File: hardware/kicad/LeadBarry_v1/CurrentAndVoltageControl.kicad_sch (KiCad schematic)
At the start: 27 parts, among them J1 Screw_Terminal_01x02, Q1 SS9014, U2 INA3221_Module, U3 LM2596S_Module

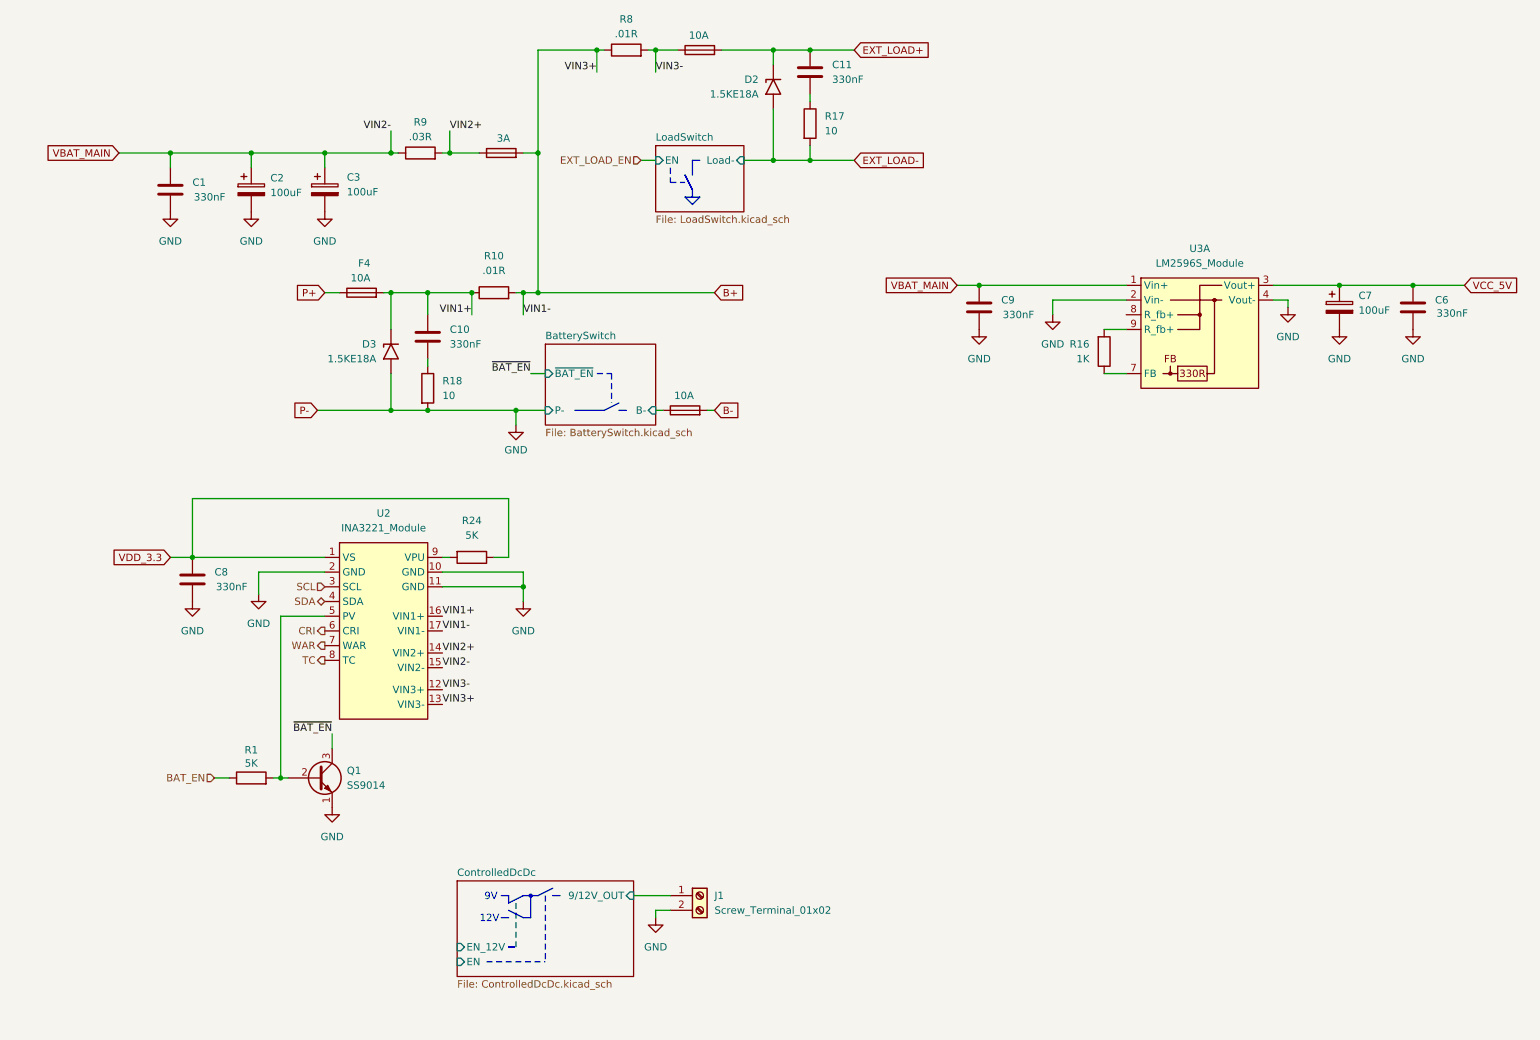
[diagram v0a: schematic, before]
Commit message: fix: pwm-controlled dc-dc output voltage
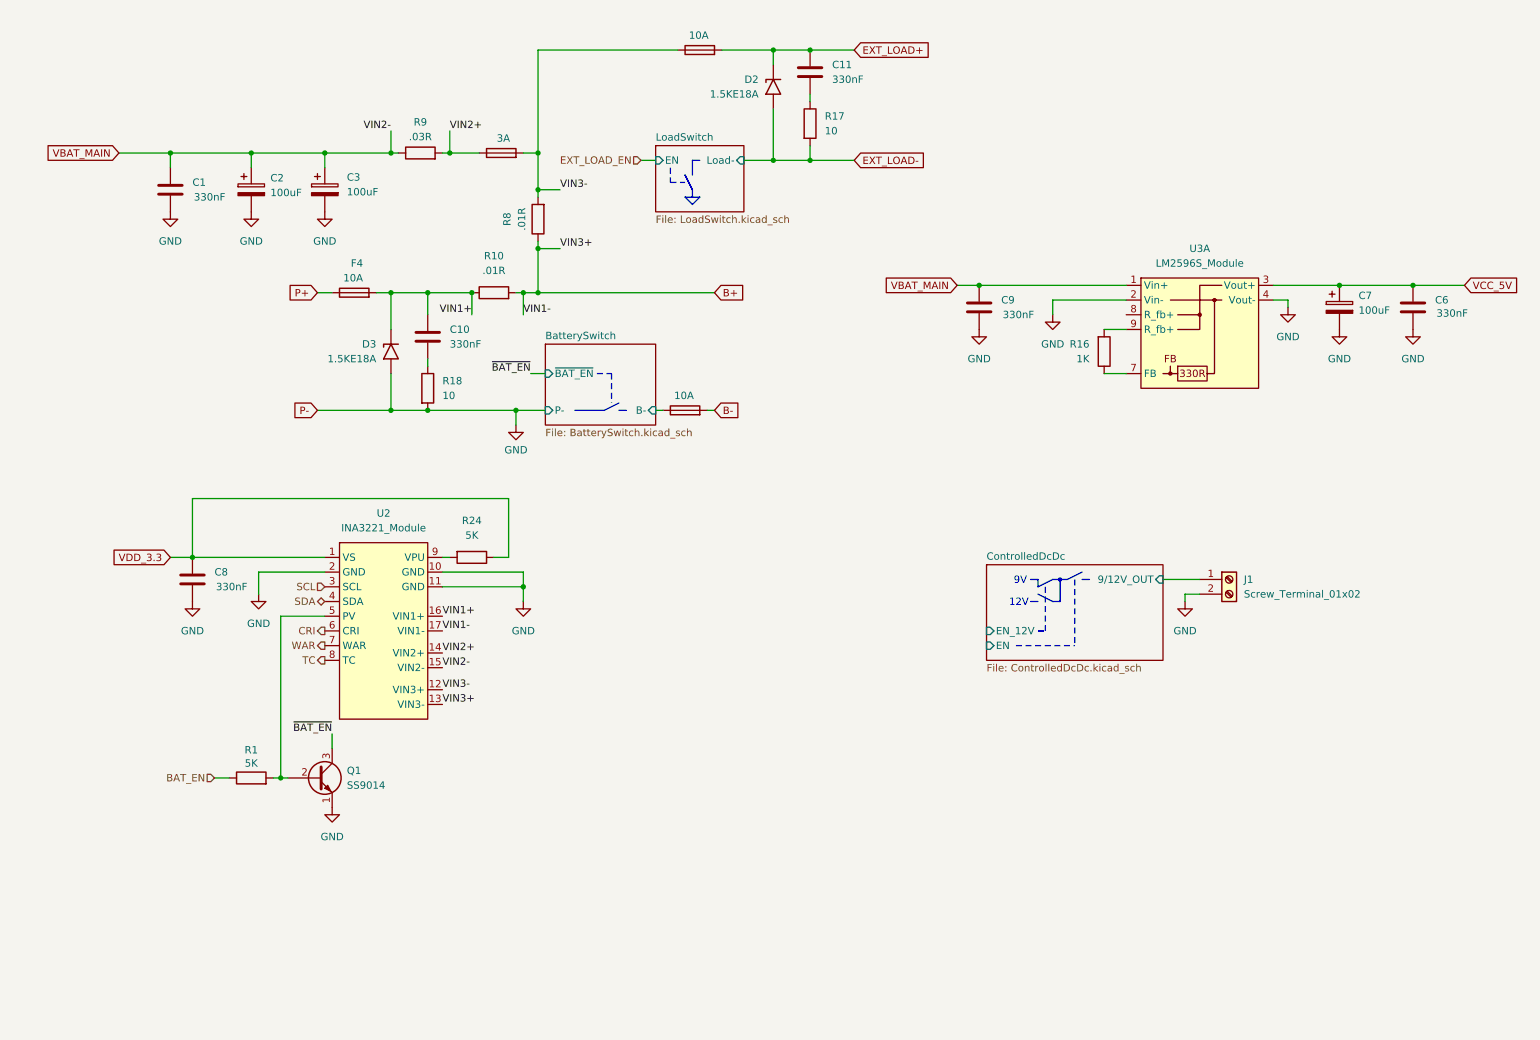
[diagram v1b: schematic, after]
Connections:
- net B+: no longer F1.2
- net VIN3-: now also F1.2
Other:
- moved on the sheet: F4, J1

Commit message: Revert "fix: pwm-controlled dc-dc output voltage"
This reverts commit b0b1c2266e3c7e9cf1a5c295a0eb9d631b1ef3e0.
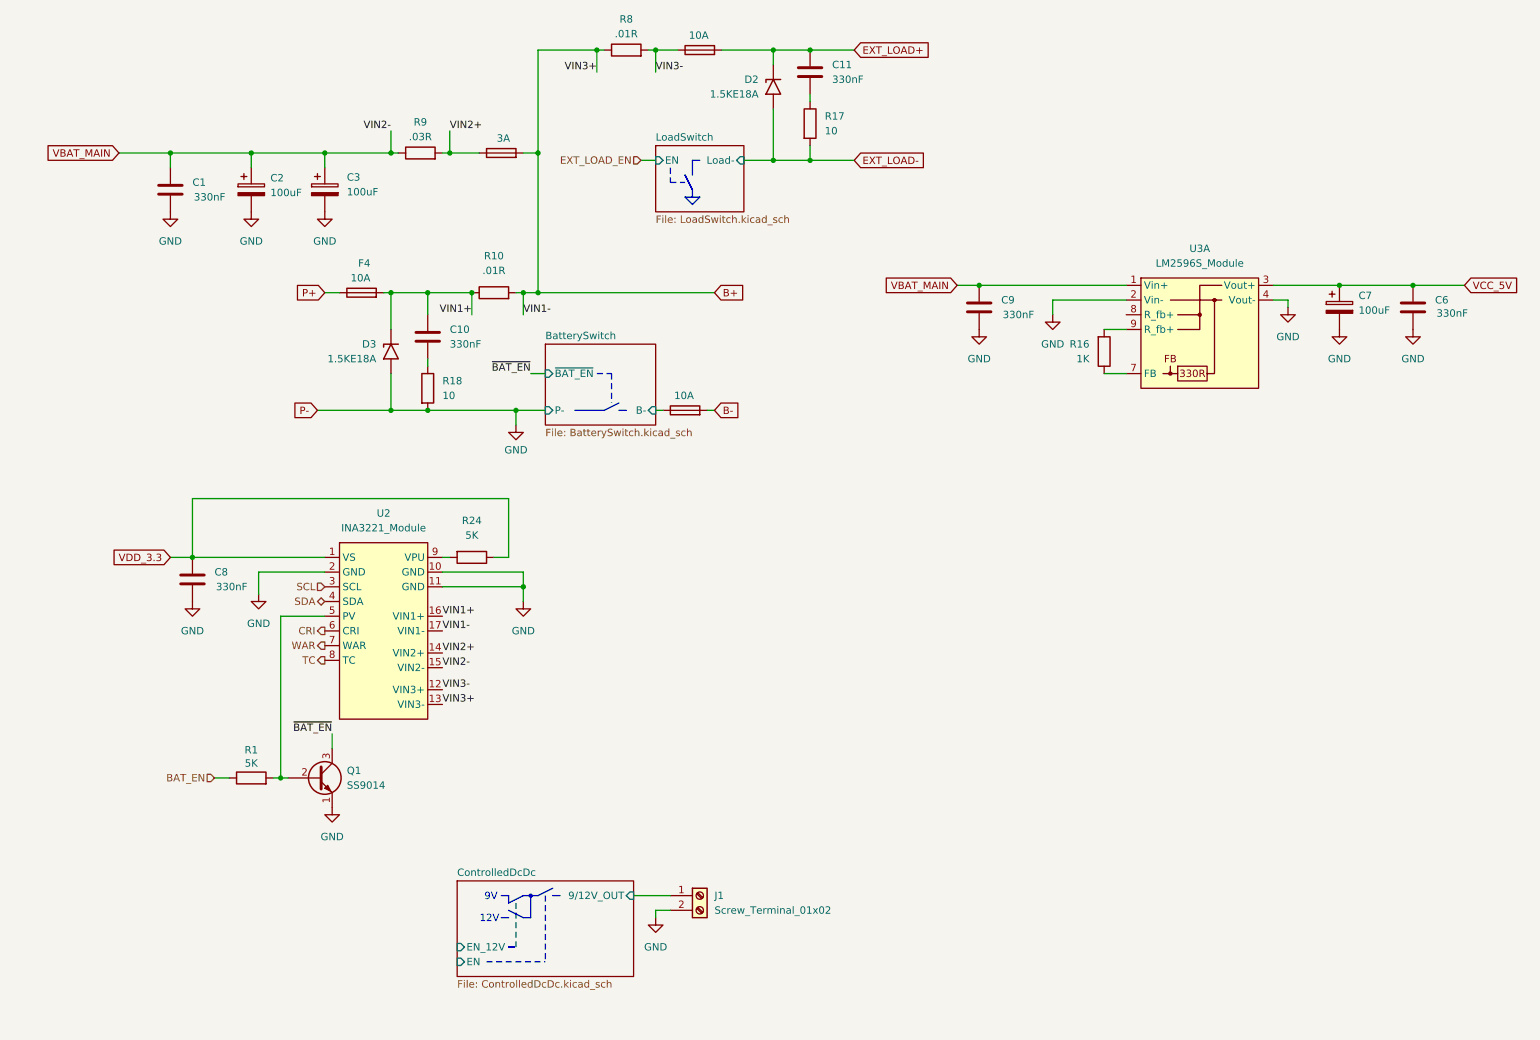
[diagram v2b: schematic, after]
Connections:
- net B+: now also F1.2
- net VIN3-: no longer F1.2
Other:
- moved on the sheet: F4, J1

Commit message: doc: refactored and enhanced
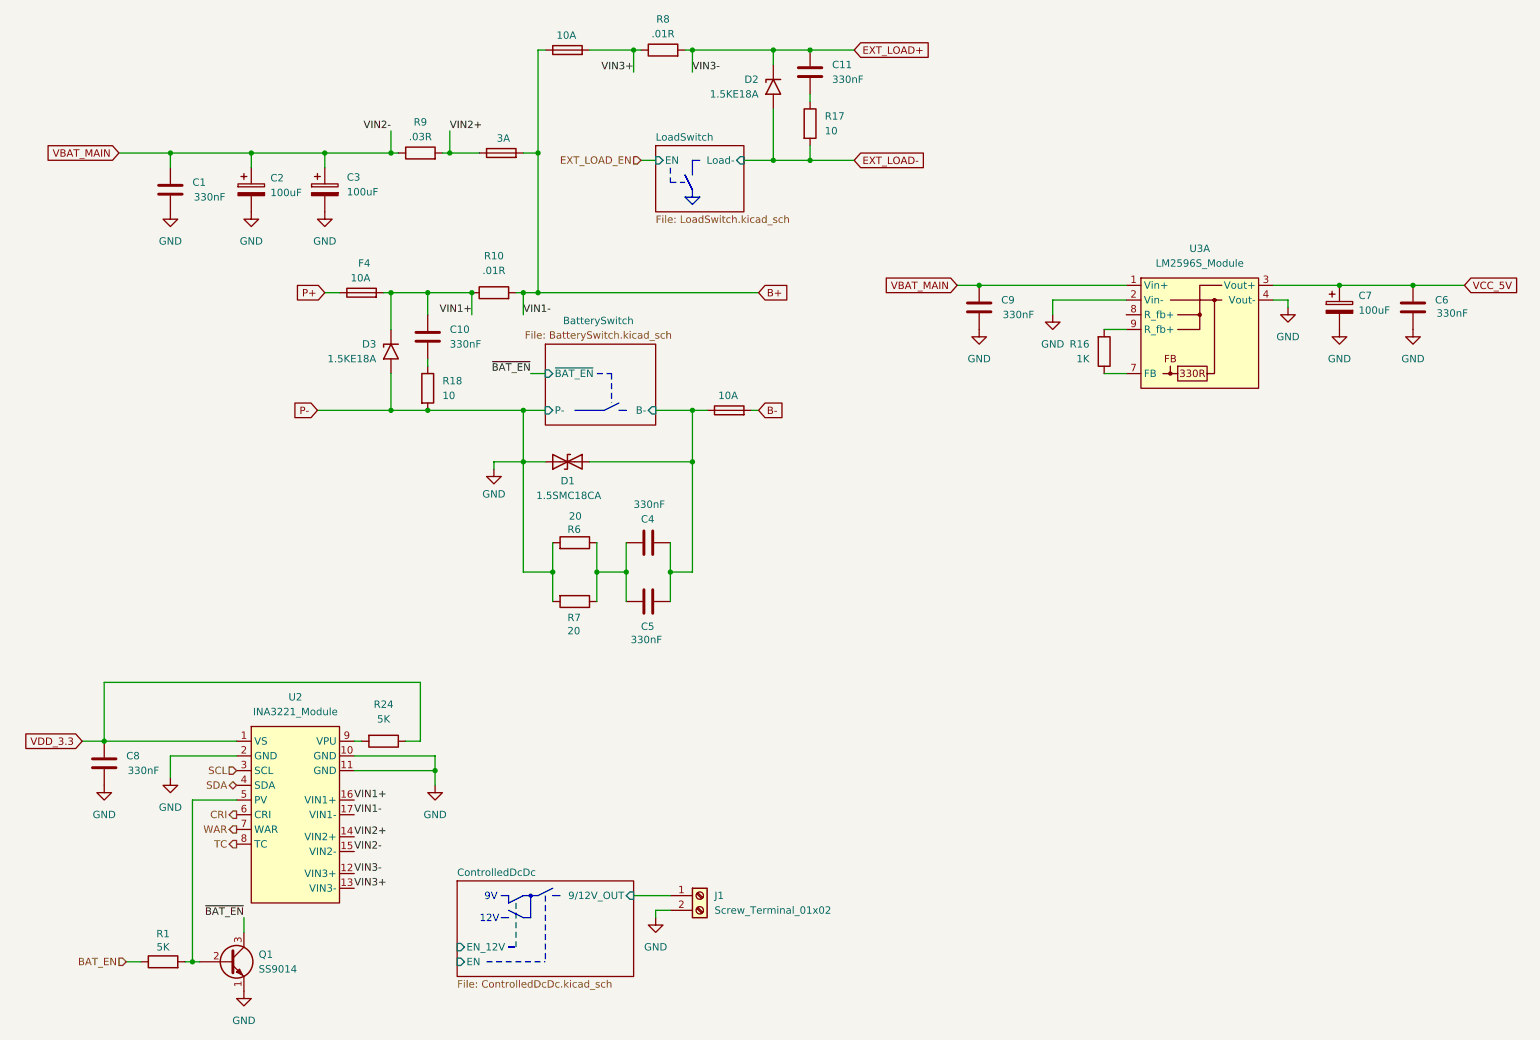
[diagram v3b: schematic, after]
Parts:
- added C4, C5: 330nF, symbol Device:C
- added D1: 1.5SMC18CA, Diode_SMD:D_SMC, symbol Diode:1.5SMC18CA
- added R6, R7: 20, Resistor_THT:R_Axial_DIN0207_L6.3mm_D2.5mm_P10.16mm_Horizontal, symbol Device:R
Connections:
- net B+: now also F3.1; no longer R8.1, U2.13 (VIN3-)
- net BatterySwitch/B-: now also C4.1, C5.1, D1.2 (A2)
- net EXT_LOAD+: now also R8.2, U2.12 (VIN3+); no longer F3.2
- net GND: now also D1.1 (A1), R6.2, R7.2
- removed net VIN3-: F3.1, R8.2, U2.12 (VIN3+)
- new net: C4.2, C5.2, R6.1, R7.1
- new net VIN3+: F3.2, R8.1, U2.13 (VIN3-)
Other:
- moved on the sheet: C8, Q1, R1, R24, R8, U2

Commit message: fix: implemented regulated voltage schematic
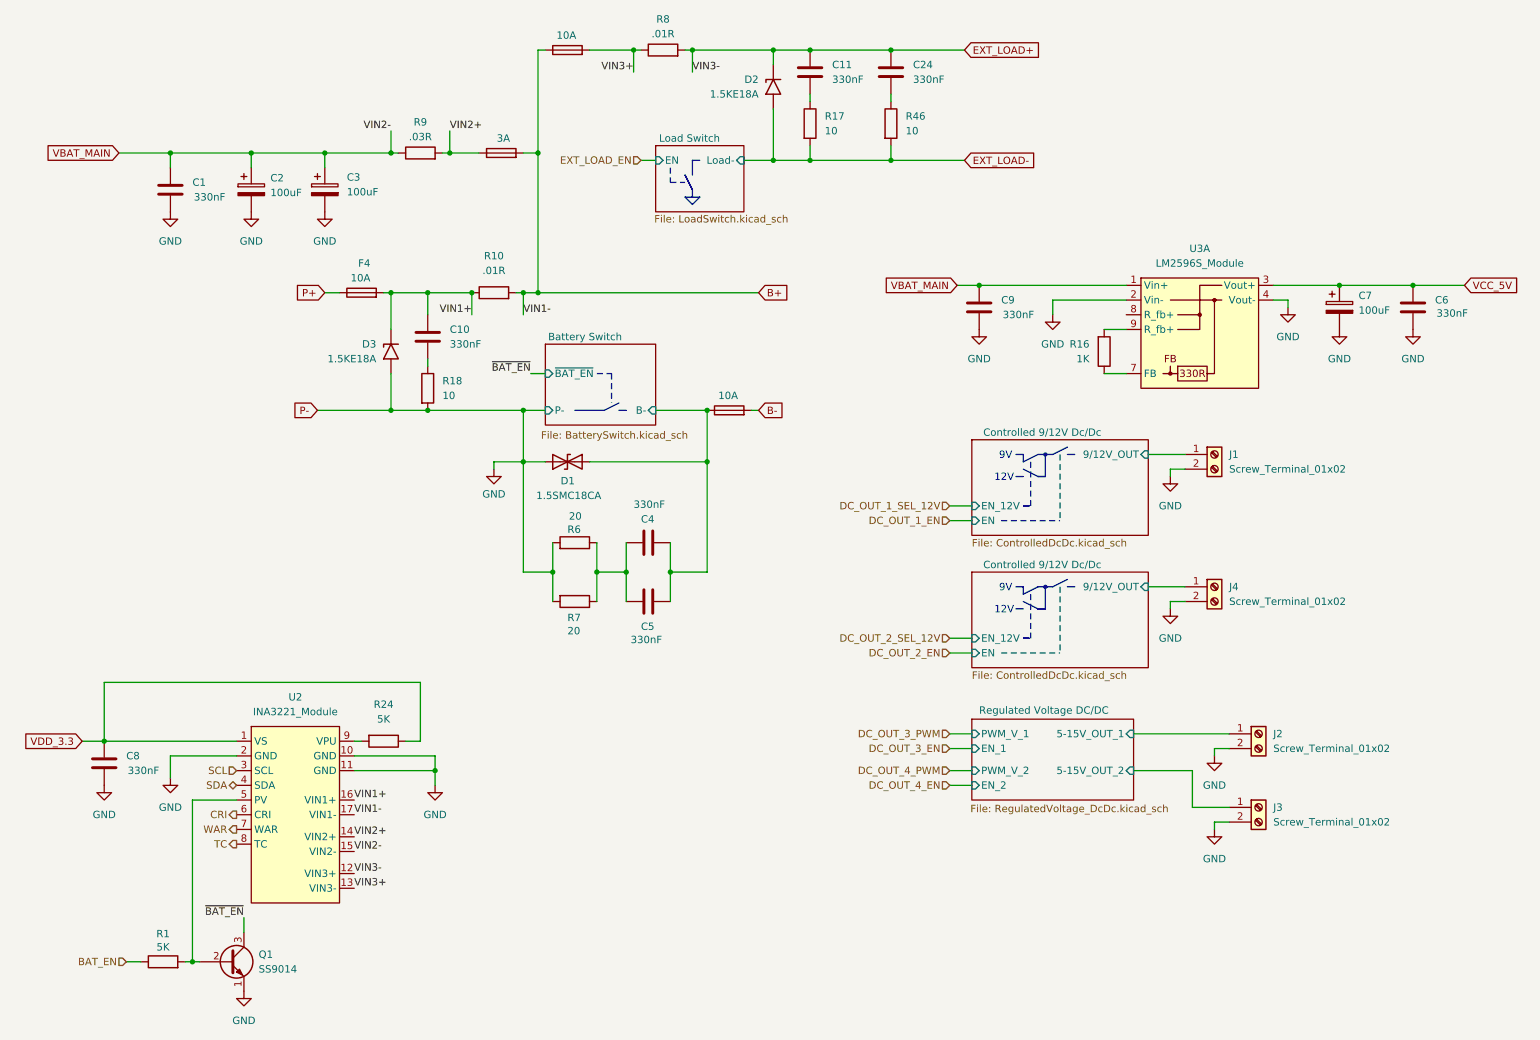
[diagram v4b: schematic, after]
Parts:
- added C24: 330nF, Capacitor_SMD:C_1206_3216Metric_Pad1.33x1.80mm_HandSolder, symbol Device:C
- added J2, J3, J4: Screw_Terminal_01x02, TerminalBlock_Phoenix:TerminalBlock_Phoenix_MKDS-1,5-2-5.08_1x02_P5.08mm_Horizontal, symbol Connector:Screw_Terminal_01x02
- added R46: 10, Resistor_THT:R_Axial_DIN0207_L6.3mm_D2.5mm_P10.16mm_Horizontal, symbol Device:R
- C1, C11, C4, C5, C6, C8, C9: footprint (none) -> Capacitor_SMD:C_1206_3216Metric_Pad1.33x1.80mm_HandSolder
- R24: footprint Resistor_THT:R_Axial_DIN0207_L6.3mm_D2.5mm_P10.16mm_Horizontal -> Resistor_SMD:R_0805_2012Metric_Pad1.20x1.40mm_HandSolder
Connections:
- net EXT_LOAD+: now also C24.1
- net EXT_LOAD-: now also R46.2
- net GND: now also J2.2 (Pin_2), J3.2 (Pin_2), J4.2 (Pin_2)
- new net: C24.2, R46.1
- new net ControlledDcDc1/9/12V_OUT: J4.1 (Pin_1)
- new net Regulated Voltage DC DC/5-15V_OUT_1: J2.1 (Pin_1)
- new net Regulated Voltage DC DC/5-15V_OUT_2: J3.1 (Pin_1)
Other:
- added sheet ControlledDcDc1 (ControlledDcDc.kicad_sch)
- added sheet Regulated Voltage DC DC (RegulatedVoltage_DcDc.kicad_sch)
- moved on the sheet: J1
